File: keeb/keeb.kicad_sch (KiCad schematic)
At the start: 162 parts, among them J101 AVR-ISP-6, J102 USB_C_Receptacle_USB2.0, SW101 SW_Push, SW102 SW_Push, SW103 SW_Push, SW104 SW_Push, SW105 SW_Push, SW106 SW_Push, SW107 SW_Push, SW108 SW_Push, SW109 SW_Push, SW110 SW_Push, SW111 SW_Push, SW112 SW_Push, SW113 SW_Push, SW114 SW_Push, SW115 SW_Push, SW116 SW_Push, SW117 SW_Push, SW118 SW_Push, SW119 SW_Push, SW120 SW_Push, SW121 SW_Push, SW122 SW_Push, SW123 SW_Push, SW124 SW_Push, SW125 SW_Push, SW126 SW_Push, SW127 SW_Push, SW128 SW_Push, SW129 SW_Push, SW130 SW_Push, SW131 SW_Push, SW132 SW_Push, SW133 SW_Push, SW134 SW_Push, SW135 SW_Push, SW136 SW_Push, SW137 SW_Push, SW138 SW_Push, SW139 SW_Push, SW140 SW_Push, SW141 SW_Push, SW142 SW_Push, SW143 SW_Push, SW144 SW_Push, SW145 SW_Push, SW146 SW_Push, SW147 SW_Push, SW148 SW_Push, SW149 SW_Push, SW150 SW_Push, SW151 SW_Push, SW152 SW_Push, SW153 SW_Push, SW154 SW_Push, SW155 SW_Push, SW156 SW_Push, SW157 SW_Push, SW158 SW_Push, SW159 SW_Push, SW160 SW_Push, SW161 SW_Push, SW162 SW_Push, SW163 SW_Push, SW164 SW_Push, SW165 SW_Push, SW166 SW_Push, SW167 SW_Push, U1 TPD2S017, U101 ATmega32U4-AU, Y101 16Mhz

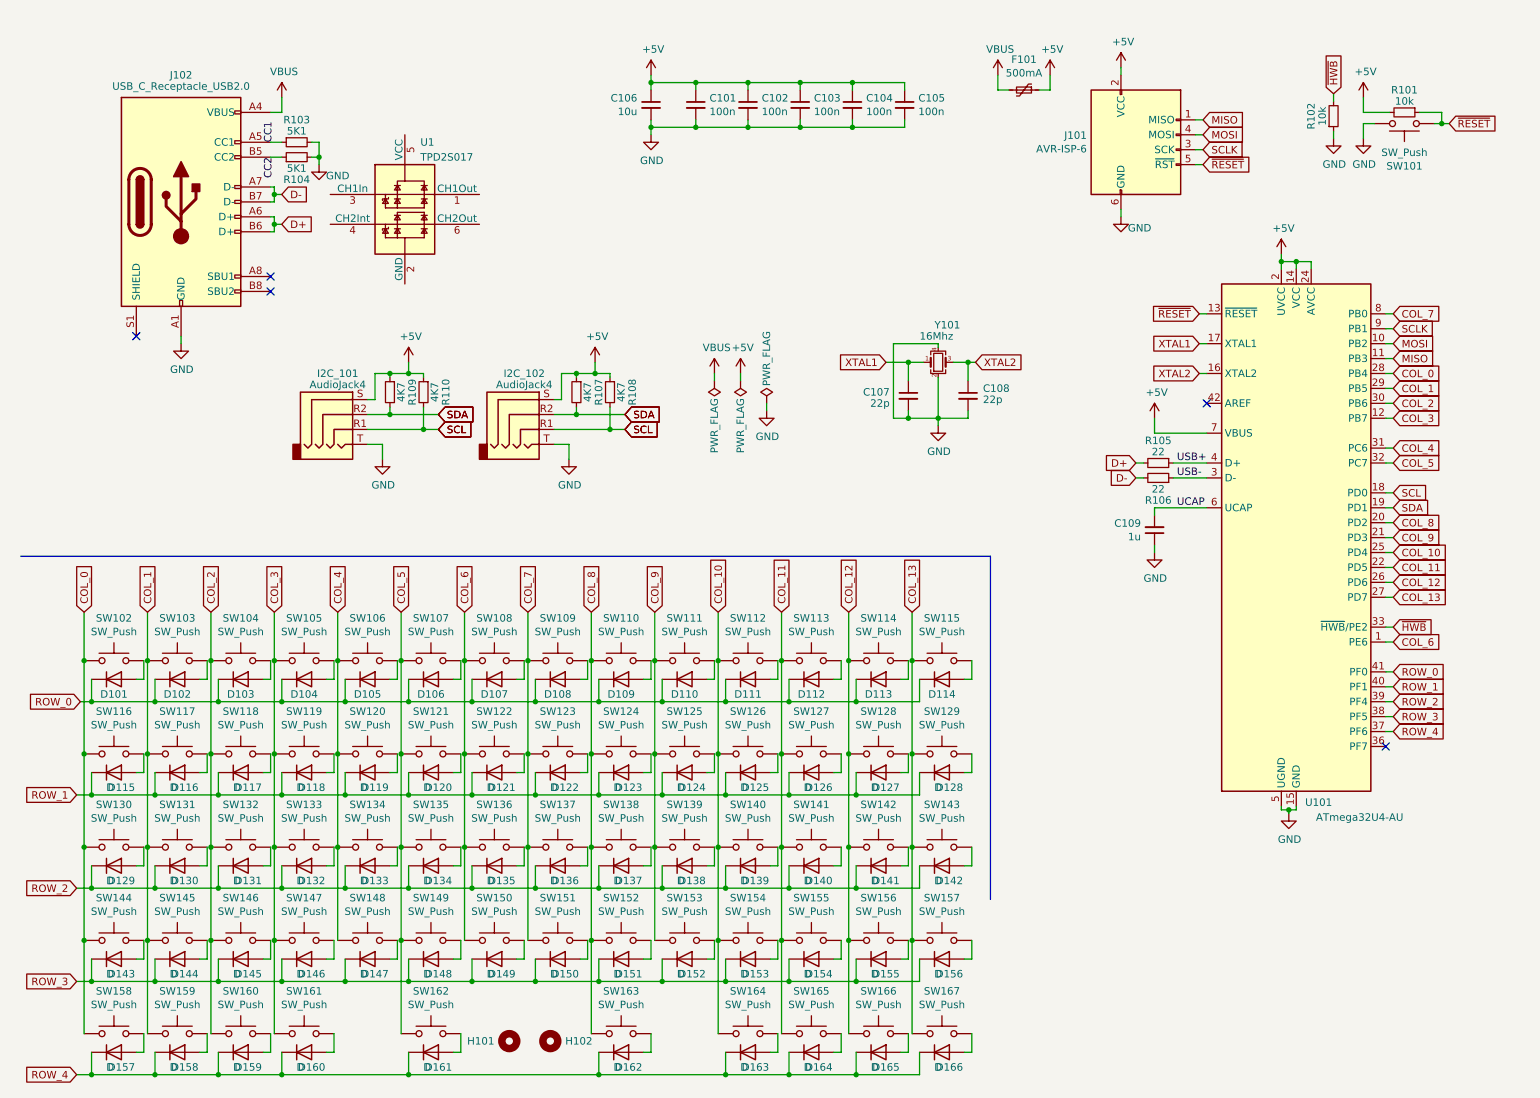
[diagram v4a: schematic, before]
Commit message: footprints/general libs redone
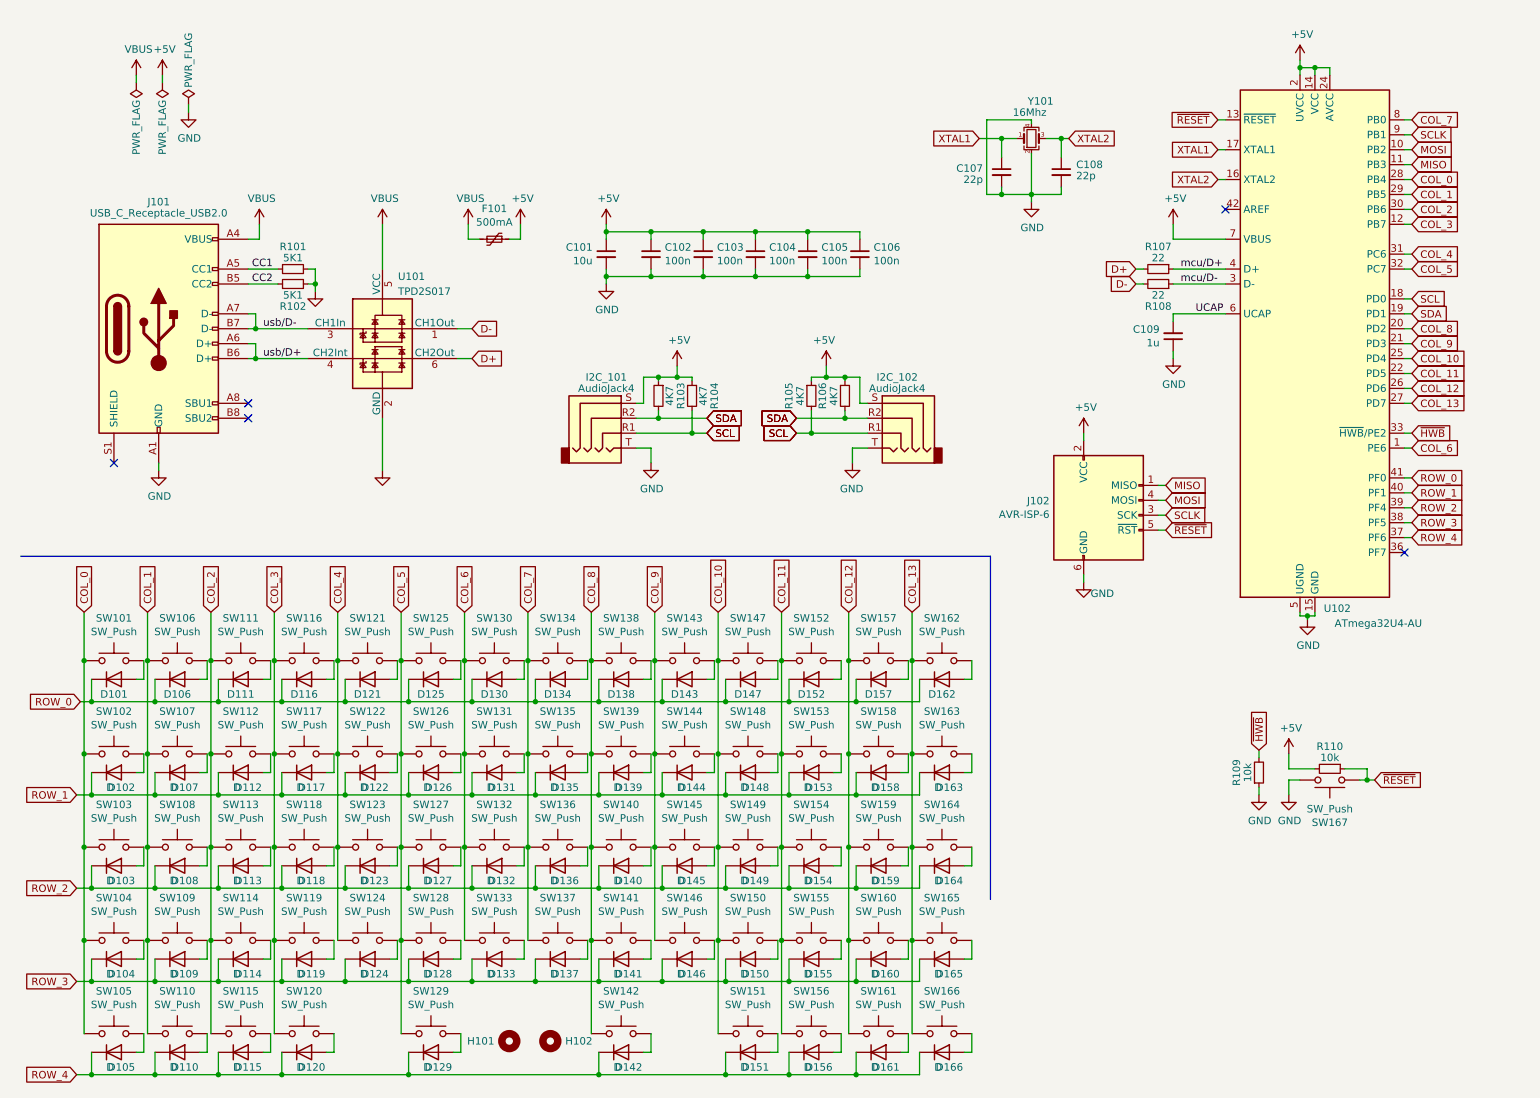
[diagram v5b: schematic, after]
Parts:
- D101, D136, D166: footprint Diode_SMD:D_SOD-123F -> Diode_SMD:D_SOD-323F
- D102: renamed from D115; footprint Diode_SMD:D_SOD-123F -> Diode_SMD:D_SOD-323F
- D103: renamed from D129; footprint Diode_SMD:D_SOD-123F -> Diode_SMD:D_SOD-323F
- D104: renamed from D143; footprint Diode_SMD:D_SOD-123F -> Diode_SMD:D_SOD-323F
- D105: renamed from D157; footprint Diode_SMD:D_SOD-123F -> Diode_SMD:D_SOD-323F
- D106: renamed from D102; footprint Diode_SMD:D_SOD-123F -> Diode_SMD:D_SOD-323F
- D107: renamed from D116; footprint Diode_SMD:D_SOD-123F -> Diode_SMD:D_SOD-323F
- D108: renamed from D130; footprint Diode_SMD:D_SOD-123F -> Diode_SMD:D_SOD-323F
- D109: renamed from D144; footprint Diode_SMD:D_SOD-123F -> Diode_SMD:D_SOD-323F
- D110: renamed from D158; footprint Diode_SMD:D_SOD-123F -> Diode_SMD:D_SOD-323F
- D111: renamed from D103; footprint Diode_SMD:D_SOD-123F -> Diode_SMD:D_SOD-323F
- D112: renamed from D117; footprint Diode_SMD:D_SOD-123F -> Diode_SMD:D_SOD-323F
- D113: renamed from D131; footprint Diode_SMD:D_SOD-123F -> Diode_SMD:D_SOD-323F
- D114: renamed from D145; footprint Diode_SMD:D_SOD-123F -> Diode_SMD:D_SOD-323F
- D115: renamed from D159; footprint Diode_SMD:D_SOD-123F -> Diode_SMD:D_SOD-323F
- D116: renamed from D104; footprint Diode_SMD:D_SOD-123F -> Diode_SMD:D_SOD-323F
- D117: renamed from D118; footprint Diode_SMD:D_SOD-123F -> Diode_SMD:D_SOD-323F
- D118: renamed from D132; footprint Diode_SMD:D_SOD-123F -> Diode_SMD:D_SOD-323F
- D119: renamed from D146; footprint Diode_SMD:D_SOD-123F -> Diode_SMD:D_SOD-323F
- D120: renamed from D160; footprint Diode_SMD:D_SOD-123F -> Diode_SMD:D_SOD-323F
- D121: renamed from D105; footprint Diode_SMD:D_SOD-123F -> Diode_SMD:D_SOD-323F
- D122: renamed from D119; footprint Diode_SMD:D_SOD-123F -> Diode_SMD:D_SOD-323F
- D123: renamed from D133; footprint Diode_SMD:D_SOD-123F -> Diode_SMD:D_SOD-323F
- D124: renamed from D147; footprint Diode_SMD:D_SOD-123F -> Diode_SMD:D_SOD-323F
- D125: renamed from D106; footprint Diode_SMD:D_SOD-123F -> Diode_SMD:D_SOD-323F
- D126: renamed from D120; footprint Diode_SMD:D_SOD-123F -> Diode_SMD:D_SOD-323F
- D127: renamed from D134; footprint Diode_SMD:D_SOD-123F -> Diode_SMD:D_SOD-323F
- D128: renamed from D148; footprint Diode_SMD:D_SOD-123F -> Diode_SMD:D_SOD-323F
- D129: renamed from D161; footprint Diode_SMD:D_SOD-123F -> Diode_SMD:D_SOD-323F
- D130: renamed from D107; footprint Diode_SMD:D_SOD-123F -> Diode_SMD:D_SOD-323F
- D131: renamed from D121; footprint Diode_SMD:D_SOD-123F -> Diode_SMD:D_SOD-323F
- D132: renamed from D135; footprint Diode_SMD:D_SOD-123F -> Diode_SMD:D_SOD-323F
- D133: renamed from D149; footprint Diode_SMD:D_SOD-123F -> Diode_SMD:D_SOD-323F
- D134: renamed from D108; footprint Diode_SMD:D_SOD-123F -> Diode_SMD:D_SOD-323F
- D135: renamed from D122; footprint Diode_SMD:D_SOD-123F -> Diode_SMD:D_SOD-323F
- D137: renamed from D150; footprint Diode_SMD:D_SOD-123F -> Diode_SMD:D_SOD-323F
- D138: renamed from D109; footprint Diode_SMD:D_SOD-123F -> Diode_SMD:D_SOD-323F
- D139: renamed from D123; footprint Diode_SMD:D_SOD-123F -> Diode_SMD:D_SOD-323F
- D140: renamed from D137; footprint Diode_SMD:D_SOD-123F -> Diode_SMD:D_SOD-323F
- D141: renamed from D151; footprint Diode_SMD:D_SOD-123F -> Diode_SMD:D_SOD-323F
- D142: renamed from D162; footprint Diode_SMD:D_SOD-123F -> Diode_SMD:D_SOD-323F
- D143: renamed from D110; footprint Diode_SMD:D_SOD-123F -> Diode_SMD:D_SOD-323F
- D144: renamed from D124; footprint Diode_SMD:D_SOD-123F -> Diode_SMD:D_SOD-323F
- D145: renamed from D138; footprint Diode_SMD:D_SOD-123F -> Diode_SMD:D_SOD-323F
- D146: renamed from D152; footprint Diode_SMD:D_SOD-123F -> Diode_SMD:D_SOD-323F
- D147: renamed from D111; footprint Diode_SMD:D_SOD-123F -> Diode_SMD:D_SOD-323F
- D148: renamed from D125; footprint Diode_SMD:D_SOD-123F -> Diode_SMD:D_SOD-323F
- D149: renamed from D139; footprint Diode_SMD:D_SOD-123F -> Diode_SMD:D_SOD-323F
- D150: renamed from D153; footprint Diode_SMD:D_SOD-123F -> Diode_SMD:D_SOD-323F
- D151: renamed from D163; footprint Diode_SMD:D_SOD-123F -> Diode_SMD:D_SOD-323F
- D152: renamed from D112; footprint Diode_SMD:D_SOD-123F -> Diode_SMD:D_SOD-323F
- D153: renamed from D126; footprint Diode_SMD:D_SOD-123F -> Diode_SMD:D_SOD-323F
- D154: renamed from D140; footprint Diode_SMD:D_SOD-123F -> Diode_SMD:D_SOD-323F
- D155: renamed from D154; footprint Diode_SMD:D_SOD-123F -> Diode_SMD:D_SOD-323F
- D156: renamed from D164; footprint Diode_SMD:D_SOD-123F -> Diode_SMD:D_SOD-323F
- D157: renamed from D113; footprint Diode_SMD:D_SOD-123F -> Diode_SMD:D_SOD-323F
- D158: renamed from D127; footprint Diode_SMD:D_SOD-123F -> Diode_SMD:D_SOD-323F
- D159: renamed from D141; footprint Diode_SMD:D_SOD-123F -> Diode_SMD:D_SOD-323F
- D160: renamed from D155; footprint Diode_SMD:D_SOD-123F -> Diode_SMD:D_SOD-323F
- D161: renamed from D165; footprint Diode_SMD:D_SOD-123F -> Diode_SMD:D_SOD-323F
- D162: renamed from D114; footprint Diode_SMD:D_SOD-123F -> Diode_SMD:D_SOD-323F
- D163: renamed from D128; footprint Diode_SMD:D_SOD-123F -> Diode_SMD:D_SOD-323F
- D164: renamed from D142; footprint Diode_SMD:D_SOD-123F -> Diode_SMD:D_SOD-323F
- D165: renamed from D156; footprint Diode_SMD:D_SOD-123F -> Diode_SMD:D_SOD-323F
- H101, H102: footprint Mounting_Keyboard_Stabilizer:Stabilizer_Cherry_MX_3u -> PCM_Mounting_Keyboard_Stabilizer:Stabilizer_Cherry_MX_3.00u
- SW102: renamed from SW116; footprint Switch_Keyboard_Cherry_MX:SW_Cherry_MX_PCB_1.00u -> PCM_Switch_Keyboard_Cherry_MX:SW_Cherry_MX_PCB_1.00u
- SW103: renamed from SW130; footprint Switch_Keyboard_Cherry_MX:SW_Cherry_MX_PCB_1.00u -> PCM_Switch_Keyboard_Cherry_MX:SW_Cherry_MX_PCB_1.00u
- SW104: renamed from SW144; footprint Switch_Keyboard_Cherry_MX:SW_Cherry_MX_PCB_1.00u -> PCM_Switch_Keyboard_Cherry_MX:SW_Cherry_MX_PCB_1.00u
- SW105: renamed from SW158; footprint Switch_Keyboard_Cherry_MX:SW_Cherry_MX_PCB_1.00u -> PCM_Switch_Keyboard_Cherry_MX:SW_Cherry_MX_PCB_1.00u
- SW106: renamed from SW103; footprint Switch_Keyboard_Cherry_MX:SW_Cherry_MX_PCB_1.00u -> PCM_Switch_Keyboard_Cherry_MX:SW_Cherry_MX_PCB_1.00u
- SW107: renamed from SW117; footprint Switch_Keyboard_Cherry_MX:SW_Cherry_MX_PCB_1.00u -> PCM_Switch_Keyboard_Cherry_MX:SW_Cherry_MX_PCB_1.00u
- SW108: renamed from SW131; footprint Switch_Keyboard_Cherry_MX:SW_Cherry_MX_PCB_1.00u -> PCM_Switch_Keyboard_Cherry_MX:SW_Cherry_MX_PCB_1.00u
- SW109: renamed from SW145; footprint Switch_Keyboard_Cherry_MX:SW_Cherry_MX_PCB_1.00u -> PCM_Switch_Keyboard_Cherry_MX:SW_Cherry_MX_PCB_1.00u
- SW110: renamed from SW159; footprint Switch_Keyboard_Cherry_MX:SW_Cherry_MX_PCB_1.00u -> PCM_Switch_Keyboard_Cherry_MX:SW_Cherry_MX_PCB_1.00u
- SW111: renamed from SW104; footprint Switch_Keyboard_Cherry_MX:SW_Cherry_MX_PCB_1.00u -> PCM_Switch_Keyboard_Cherry_MX:SW_Cherry_MX_PCB_1.00u
- SW112: renamed from SW118; footprint Switch_Keyboard_Cherry_MX:SW_Cherry_MX_PCB_1.00u -> PCM_Switch_Keyboard_Cherry_MX:SW_Cherry_MX_PCB_1.00u
- SW113: renamed from SW132; footprint Switch_Keyboard_Cherry_MX:SW_Cherry_MX_PCB_1.00u -> PCM_Switch_Keyboard_Cherry_MX:SW_Cherry_MX_PCB_1.00u
- SW114: renamed from SW146; footprint Switch_Keyboard_Cherry_MX:SW_Cherry_MX_PCB_1.00u -> PCM_Switch_Keyboard_Cherry_MX:SW_Cherry_MX_PCB_1.00u
- SW115: renamed from SW160; footprint Switch_Keyboard_Cherry_MX:SW_Cherry_MX_PCB_1.00u -> PCM_Switch_Keyboard_Cherry_MX:SW_Cherry_MX_PCB_1.00u
- SW116: renamed from SW105; footprint Switch_Keyboard_Cherry_MX:SW_Cherry_MX_PCB_1.00u -> PCM_Switch_Keyboard_Cherry_MX:SW_Cherry_MX_PCB_1.00u
- SW117: renamed from SW119; footprint Switch_Keyboard_Cherry_MX:SW_Cherry_MX_PCB_1.00u -> PCM_Switch_Keyboard_Cherry_MX:SW_Cherry_MX_PCB_1.00u
- SW118: renamed from SW133; footprint Switch_Keyboard_Cherry_MX:SW_Cherry_MX_PCB_1.00u -> PCM_Switch_Keyboard_Cherry_MX:SW_Cherry_MX_PCB_1.00u
- SW119: renamed from SW147; footprint Switch_Keyboard_Cherry_MX:SW_Cherry_MX_PCB_1.00u -> PCM_Switch_Keyboard_Cherry_MX:SW_Cherry_MX_PCB_1.00u
- SW120: renamed from SW161; footprint Switch_Keyboard_Cherry_MX:SW_Cherry_MX_PCB_1.00u -> PCM_Switch_Keyboard_Cherry_MX:SW_Cherry_MX_PCB_1.00u
- SW121: renamed from SW106; footprint Switch_Keyboard_Cherry_MX:SW_Cherry_MX_PCB_1.00u -> PCM_Switch_Keyboard_Cherry_MX:SW_Cherry_MX_PCB_1.00u
- SW122: renamed from SW120; footprint Switch_Keyboard_Cherry_MX:SW_Cherry_MX_PCB_1.00u -> PCM_Switch_Keyboard_Cherry_MX:SW_Cherry_MX_PCB_1.00u
- SW123: renamed from SW134; footprint Switch_Keyboard_Cherry_MX:SW_Cherry_MX_PCB_1.00u -> PCM_Switch_Keyboard_Cherry_MX:SW_Cherry_MX_PCB_1.00u
- SW124: renamed from SW148; footprint Switch_Keyboard_Cherry_MX:SW_Cherry_MX_PCB_1.00u -> PCM_Switch_Keyboard_Cherry_MX:SW_Cherry_MX_PCB_1.00u
- SW125: renamed from SW107; footprint Switch_Keyboard_Cherry_MX:SW_Cherry_MX_PCB_1.00u -> PCM_Switch_Keyboard_Cherry_MX:SW_Cherry_MX_PCB_1.00u
- SW126: renamed from SW121; footprint Switch_Keyboard_Cherry_MX:SW_Cherry_MX_PCB_1.00u -> PCM_Switch_Keyboard_Cherry_MX:SW_Cherry_MX_PCB_1.00u
- SW127: renamed from SW135; footprint Switch_Keyboard_Cherry_MX:SW_Cherry_MX_PCB_1.00u -> PCM_Switch_Keyboard_Cherry_MX:SW_Cherry_MX_PCB_1.00u
- SW128: renamed from SW149; footprint Switch_Keyboard_Cherry_MX:SW_Cherry_MX_PCB_1.00u -> PCM_Switch_Keyboard_Cherry_MX:SW_Cherry_MX_PCB_1.00u
- SW129: renamed from SW162; footprint Switch_Keyboard_Cherry_MX:SW_Cherry_MX_PCB_3.00u -> PCM_Switch_Keyboard_Cherry_MX:SW_Cherry_MX_PCB_3.00u
- SW130: renamed from SW108; footprint Switch_Keyboard_Cherry_MX:SW_Cherry_MX_PCB_1.00u -> PCM_Switch_Keyboard_Cherry_MX:SW_Cherry_MX_PCB_1.00u
- SW131: renamed from SW122; footprint Switch_Keyboard_Cherry_MX:SW_Cherry_MX_PCB_1.00u -> PCM_Switch_Keyboard_Cherry_MX:SW_Cherry_MX_PCB_1.00u
- SW132: renamed from SW136; footprint Switch_Keyboard_Cherry_MX:SW_Cherry_MX_PCB_1.00u -> PCM_Switch_Keyboard_Cherry_MX:SW_Cherry_MX_PCB_1.00u
- SW133: renamed from SW150; footprint Switch_Keyboard_Cherry_MX:SW_Cherry_MX_PCB_1.00u -> PCM_Switch_Keyboard_Cherry_MX:SW_Cherry_MX_PCB_1.00u
- SW134: renamed from SW109; footprint Switch_Keyboard_Cherry_MX:SW_Cherry_MX_PCB_1.00u -> PCM_Switch_Keyboard_Cherry_MX:SW_Cherry_MX_PCB_1.00u
- SW135: renamed from SW123; footprint Switch_Keyboard_Cherry_MX:SW_Cherry_MX_PCB_1.00u -> PCM_Switch_Keyboard_Cherry_MX:SW_Cherry_MX_PCB_1.00u
- SW136: renamed from SW137; footprint Switch_Keyboard_Cherry_MX:SW_Cherry_MX_PCB_1.00u -> PCM_Switch_Keyboard_Cherry_MX:SW_Cherry_MX_PCB_1.00u
- SW137: renamed from SW151; footprint Switch_Keyboard_Cherry_MX:SW_Cherry_MX_PCB_1.00u -> PCM_Switch_Keyboard_Cherry_MX:SW_Cherry_MX_PCB_1.00u
- SW138: renamed from SW110; footprint Switch_Keyboard_Cherry_MX:SW_Cherry_MX_PCB_1.00u -> PCM_Switch_Keyboard_Cherry_MX:SW_Cherry_MX_PCB_1.00u
- SW139: renamed from SW124; footprint Switch_Keyboard_Cherry_MX:SW_Cherry_MX_PCB_1.00u -> PCM_Switch_Keyboard_Cherry_MX:SW_Cherry_MX_PCB_1.00u
- SW140: renamed from SW138; footprint Switch_Keyboard_Cherry_MX:SW_Cherry_MX_PCB_1.00u -> PCM_Switch_Keyboard_Cherry_MX:SW_Cherry_MX_PCB_1.00u
- SW141: renamed from SW152; footprint Switch_Keyboard_Cherry_MX:SW_Cherry_MX_PCB_1.00u -> PCM_Switch_Keyboard_Cherry_MX:SW_Cherry_MX_PCB_1.00u
- SW142: renamed from SW163; footprint Switch_Keyboard_Cherry_MX:SW_Cherry_MX_PCB_3.00u -> PCM_Switch_Keyboard_Cherry_MX:SW_Cherry_MX_PCB_3.00u
- SW143: renamed from SW111; footprint Switch_Keyboard_Cherry_MX:SW_Cherry_MX_PCB_1.00u -> PCM_Switch_Keyboard_Cherry_MX:SW_Cherry_MX_PCB_1.00u
- SW144: renamed from SW125; footprint Switch_Keyboard_Cherry_MX:SW_Cherry_MX_PCB_1.00u -> PCM_Switch_Keyboard_Cherry_MX:SW_Cherry_MX_PCB_1.00u
- SW145: renamed from SW139; footprint Switch_Keyboard_Cherry_MX:SW_Cherry_MX_PCB_1.00u -> PCM_Switch_Keyboard_Cherry_MX:SW_Cherry_MX_PCB_1.00u
- SW146: renamed from SW153; footprint Switch_Keyboard_Cherry_MX:SW_Cherry_MX_PCB_1.00u -> PCM_Switch_Keyboard_Cherry_MX:SW_Cherry_MX_PCB_1.00u
- SW147: renamed from SW112; footprint Switch_Keyboard_Cherry_MX:SW_Cherry_MX_PCB_1.00u -> PCM_Switch_Keyboard_Cherry_MX:SW_Cherry_MX_PCB_1.00u
- SW148: renamed from SW126; footprint Switch_Keyboard_Cherry_MX:SW_Cherry_MX_PCB_1.00u -> PCM_Switch_Keyboard_Cherry_MX:SW_Cherry_MX_PCB_1.00u
- SW149: renamed from SW140; footprint Switch_Keyboard_Cherry_MX:SW_Cherry_MX_PCB_1.00u -> PCM_Switch_Keyboard_Cherry_MX:SW_Cherry_MX_PCB_1.00u
- SW150: renamed from SW154; footprint Switch_Keyboard_Cherry_MX:SW_Cherry_MX_PCB_1.00u -> PCM_Switch_Keyboard_Cherry_MX:SW_Cherry_MX_PCB_1.00u
- SW151: renamed from SW164; footprint Switch_Keyboard_Cherry_MX:SW_Cherry_MX_PCB_1.00u -> PCM_Switch_Keyboard_Cherry_MX:SW_Cherry_MX_PCB_1.00u
- SW152: renamed from SW113; footprint Switch_Keyboard_Cherry_MX:SW_Cherry_MX_PCB_1.00u -> PCM_Switch_Keyboard_Cherry_MX:SW_Cherry_MX_PCB_1.00u
- SW153: renamed from SW127; footprint Switch_Keyboard_Cherry_MX:SW_Cherry_MX_PCB_1.00u -> PCM_Switch_Keyboard_Cherry_MX:SW_Cherry_MX_PCB_1.00u
- SW154: renamed from SW141; footprint Switch_Keyboard_Cherry_MX:SW_Cherry_MX_PCB_1.00u -> PCM_Switch_Keyboard_Cherry_MX:SW_Cherry_MX_PCB_1.00u
- SW155: footprint Switch_Keyboard_Cherry_MX:SW_Cherry_MX_PCB_1.00u -> PCM_Switch_Keyboard_Cherry_MX:SW_Cherry_MX_PCB_1.00u
- SW156: renamed from SW165; footprint Switch_Keyboard_Cherry_MX:SW_Cherry_MX_PCB_1.00u -> PCM_Switch_Keyboard_Cherry_MX:SW_Cherry_MX_PCB_1.00u
- SW157: renamed from SW114; footprint Switch_Keyboard_Cherry_MX:SW_Cherry_MX_PCB_1.00u -> PCM_Switch_Keyboard_Cherry_MX:SW_Cherry_MX_PCB_1.00u
- SW158: renamed from SW128; footprint Switch_Keyboard_Cherry_MX:SW_Cherry_MX_PCB_1.00u -> PCM_Switch_Keyboard_Cherry_MX:SW_Cherry_MX_PCB_1.00u
- SW159: renamed from SW142; footprint Switch_Keyboard_Cherry_MX:SW_Cherry_MX_PCB_1.00u -> PCM_Switch_Keyboard_Cherry_MX:SW_Cherry_MX_PCB_1.00u
- SW160: renamed from SW156; footprint Switch_Keyboard_Cherry_MX:SW_Cherry_MX_PCB_1.00u -> PCM_Switch_Keyboard_Cherry_MX:SW_Cherry_MX_PCB_1.00u
- SW161: renamed from SW166; footprint Switch_Keyboard_Cherry_MX:SW_Cherry_MX_PCB_1.00u -> PCM_Switch_Keyboard_Cherry_MX:SW_Cherry_MX_PCB_1.00u
- SW162: renamed from SW115; footprint Switch_Keyboard_Cherry_MX:SW_Cherry_MX_PCB_1.00u -> PCM_Switch_Keyboard_Cherry_MX:SW_Cherry_MX_PCB_1.00u
- SW163: renamed from SW129; footprint Switch_Keyboard_Cherry_MX:SW_Cherry_MX_PCB_1.00u -> PCM_Switch_Keyboard_Cherry_MX:SW_Cherry_MX_PCB_1.00u
- SW164: renamed from SW143; footprint Switch_Keyboard_Cherry_MX:SW_Cherry_MX_PCB_1.00u -> PCM_Switch_Keyboard_Cherry_MX:SW_Cherry_MX_PCB_1.00u
- SW165: renamed from SW157; footprint Switch_Keyboard_Cherry_MX:SW_Cherry_MX_PCB_1.00u -> PCM_Switch_Keyboard_Cherry_MX:SW_Cherry_MX_PCB_1.00u
- SW166: renamed from SW167; footprint Switch_Keyboard_Cherry_MX:SW_Cherry_MX_PCB_1.00u -> PCM_Switch_Keyboard_Cherry_MX:SW_Cherry_MX_PCB_1.00u
- renumbered C106 to C101, C101 to C102, C102 to C103, C103 to C104, C104 to C105, C105 to C106, I2C_102 to I2C_101, I2C_101 to I2C_102, J102 to J101, J101 to J102, R103 to R101, R104 to R102, R107 to R103, R108 to R104, R110 to R105, R109 to R106, R105 to R107, R106 to R108, R102 to R109, R101 to R110, SW102 to SW101, SW101 to SW167, U1 to U101, U101 to U102
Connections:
- net D+: now also U101.6 (CH2Out); no longer J101.A6 (D+), J101.B6 (D+)
- net D-: now also U101.1 (CH1Out); no longer J101.A7 (D-), J101.B7 (D-)
- net GND: now also U101.2 (GND)
- net VBUS: now also U101.5 (VCC)
- net usb/D-: now reaches U101.3 (CH1In)
- net usb/D-: now also J101.A7 (D-), J101.B7 (D-)
- net usb/D+: now reaches U101.4 (CH2Int)
- net usb/D+: now also J101.A6 (D+), J101.B6 (D+)
- net USB+ renamed mcu/D+
- net USB- renamed mcu/D-
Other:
- moved on the sheet: C101, C102, C103, C104, C105, C106, C107, C108, C109, F101, I2C_101, I2C_102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

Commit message: matrix and row/colrouting
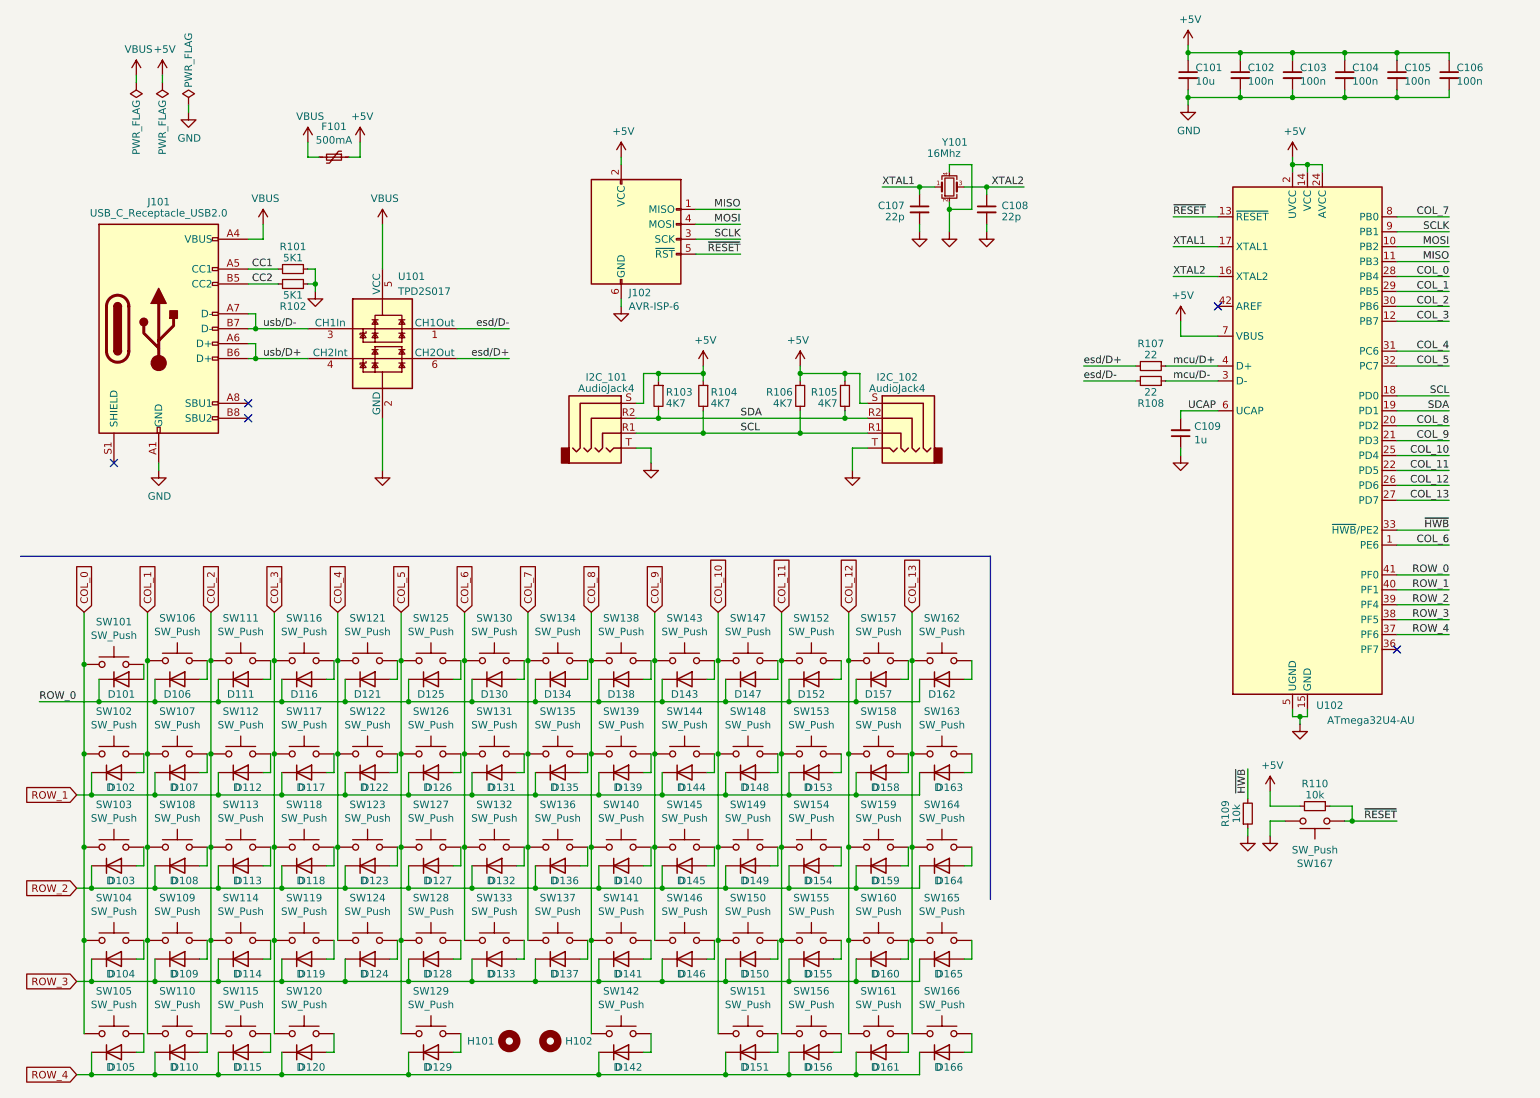
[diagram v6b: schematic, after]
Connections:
- net SCL: now also R106.2; no longer R105.2
- net SDA: now also R105.2; no longer R106.2
- net D+ renamed esd/D+
- net D- renamed esd/D-
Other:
- moved on the sheet: C101, C102, C103, C104, C105, C106, C107, C108, C109, D101, F101, J102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

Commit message: USB
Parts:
- C102, C103, C104, C105, C106, C107, C108, C109: footprint Capacitor_SMD:C_0603_1608Metric_Pad1.08x0.95mm_HandSolder -> Capacitor_SMD:C_0402_1005Metric
- R101, R102, R103, R104, R105, R106, R107, R108, R109, R110: footprint Resistor_SMD:R_0603_1608Metric_Pad0.98x0.95mm_HandSolder -> Resistor_SMD:R_0402_1005Metric
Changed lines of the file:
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@@
       (effects (font (size 1.27 1.27)))
     )
-    (property "Footprint" "Resistor_SMD:R_0603_1608Metric_Pad0.98x0.95mm_HandSolder" (at 204.47 74.93 0)
+    (property "Footprint" "Resistor_SMD:R_0402_1005Metric" (at 204.47 74.93 0)
       (effects (font (size 1.27 1.27)) hide)
     )
@@
       (effects (font (size 1.27 1.27)))
     )
-    (property "Footprint" "Resistor_SMD:R_0603_1608Metric_Pad0.98x0.95mm_HandSolder" (at 204.47 77.47 0)
+    (property "Footprint" "Resistor_SMD:R_0402_1005Metric" (at 204.47 77.47 0)
       (effects (font (size 1.27 1.27)) hide)
     )
@@
       (effects (font (size 1.27 1.27)) (justify right))
     )
-    (property "Footprint" "Resistor_SMD:R_0603_1608Metric_Pad0.98x0.95mm_HandSolder" (at 120.65 80.01 0)
+    (property "Footprint" "Resistor_SMD:R_0402_1005Metric" (at 120.65 80.01 0)
       (effects (font (size 1.27 1.27)) hide)
     )
@@
       (effects (font (size 1.27 1.27)))
     )
-    (property "Footprint" "Resistor_SMD:R_0603_1608Metric_Pad0.98x0.95mm_HandSolder" (at 58.42 60.96 0)
+    (property "Footprint" "Resistor_SMD:R_0402_1005Metric" (at 58.42 60.96 0)
       (effects (font (size 1.27 1.27)) hide)
     )
@@
       (effects (font (size 1.27 1.27)))
     )
-    (property "Footprint" "Resistor_SMD:R_0603_1608Metric_Pad0.98x0.95mm_HandSolder" (at 58.42 58.42 0)
+    (property "Footprint" "Resistor_SMD:R_0402_1005Metric" (at 58.42 58.42 0)
       (effects (font (size 1.27 1.27)) hide)
     )
@@
       (effects (font (size 1.27 1.27)) (justify right))
     )
-    (property "Footprint" "Capacitor_SMD:C_0603_1608Metric_Pad1.08x0.95mm_HandSolder" (at 209.55 86.36 0)
+    (property "Footprint" "Capacitor_SMD:C_0402_1005Metric" (at 209.55 86.36 0)
       (effects (font (size 1.27 1.27)) hide)
     )
@@
       (effects (font (size 1.27 1.27)) (justify left))
     )
-    (property "Footprint" "Capacitor_SMD:C_0603_1608Metric_Pad1.08x0.95mm_HandSolder" (at 219.71 25.4 0)
+    (property "Footprint" "Capacitor_SMD:C_0402_1005Metric" (at 219.71 25.4 0)
       (effects (font (size 1.27 1.27)) hide)
     )
@@
       (effects (font (size 1.27 1.27)) (justify left))
     )
-    (property "Footprint" "Capacitor_SMD:C_0603_1608Metric_Pad1.08x0.95mm_HandSolder" (at 228.6 25.4 0)
+    (property "Footprint" "Capacitor_SMD:C_0402_1005Metric" (at 228.6 25.4 0)
       (effects (font (size 1.27 1.27)) hide)
     )
@@
       (effects (font (size 1.27 1.27)) (justify left))
     )
-    (property "Footprint" "Capacitor_SMD:C_0603_1608Metric_Pad1.08x0.95mm_HandSolder" (at 237.49 25.4 0)
+    (property "Footprint" "Capacitor_SMD:C_0402_1005Metric" (at 237.49 25.4 0)
       (effects (font (size 1.27 1.27)) hide)
     )
@@
       (effects (font (size 1.27 1.27)) (justify left))
     )
-    (property "Footprint" "Capacitor_SMD:C_0603_1608Metric_Pad1.08x0.95mm_HandSolder" (at 246.38 25.4 0)
+    (property "Footprint" "Capacitor_SMD:C_0402_1005Metric" (at 246.38 25.4 0)
       (effects (font (size 1.27 1.27)) hide)
     )
@@
       (effects (font (size 1.27 1.27)) (justify left))
     )
-    (property "Footprint" "Capacitor_SMD:C_0603_1608Metric_Pad1.08x0.95mm_HandSolder" (at 255.27 25.4 0)
+    (property "Footprint" "Capacitor_SMD:C_0402_1005Metric" (at 255.27 25.4 0)
       (effects (font (size 1.27 1.27)) hide)
     )
@@
       (effects (font (size 1.27 1.27)) (justify right))
     )
-    (property "Footprint" "Capacitor_SMD:C_0603_1608Metric_Pad1.08x0.95mm_HandSolder" (at 165.1 48.26 0)
+    (property "Footprint" "Capacitor_SMD:C_0402_1005Metric" (at 165.1 48.26 0)
       (effects (font (size 1.27 1.27)) hide)
     )
@@
       (effects (font (size 1.27 1.27)) (justify right))
     )
-    (property "Footprint" "Capacitor_SMD:C_0603_1608Metric_Pad1.08x0.95mm_HandSolder" (at 176.53 48.26 0)
+    (property "Footprint" "Capacitor_SMD:C_0402_1005Metric" (at 176.53 48.26 0)
       (effects (font (size 1.27 1.27)) hide)
     )
@@
       (effects (font (size 1.27 1.27)))
     )
-    (property "Footprint" "Resistor_SMD:R_0603_1608Metric_Pad0.98x0.95mm_HandSolder" (at 232.41 149.86 0)
+    (property "Footprint" "Resistor_SMD:R_0402_1005Metric" (at 232.41 149.86 0)
       (effects (font (size 1.27 1.27)) hide)
     )
@@
       (effects (font (size 1.27 1.27)))
     )
-    (property "Footprint" "Resistor_SMD:R_0603_1608Metric_Pad0.98x0.95mm_HandSolder" (at 220.98 151.13 0)
+    (property "Footprint" "Resistor_SMD:R_0402_1005Metric" (at 220.98 151.13 0)
       (effects (font (size 1.27 1.27)) hide)
     )
@@
       (effects (font (size 1.27 1.27)) (justify right))
     )
-    (property "Footprint" "Resistor_SMD:R_0603_1608Metric_Pad0.98x0.95mm_HandSolder" (at 152.4 80.01 0)
+    (property "Footprint" "Resistor_SMD:R_0402_1005Metric" (at 152.4 80.01 0)
       (effects (font (size 1.27 1.27)) hide)
     )
@@
       (effects (font (size 1.27 1.27)) (justify right))
     )
-    (property "Footprint" "Resistor_SMD:R_0603_1608Metric_Pad0.98x0.95mm_HandSolder" (at 128.27 80.01 0)
+    (property "Footprint" "Resistor_SMD:R_0402_1005Metric" (at 128.27 80.01 0)
       (effects (font (size 1.27 1.27)) hide)
     )
@@
       (effects (font (size 1.27 1.27)) (justify right))
     )
-    (property "Footprint" "Resistor_SMD:R_0603_1608Metric_Pad0.98x0.95mm_HandSolder" (at 144.78 80.01 0)
-      (effects (font (size 1.27 1.27)) hide)
-    )
+    (property "Footprint" "Resistor_SMD:R_0402_1005Metric" (at 144.78 80.01 0)
+      (effects (font (size 1.27 1.27)) hide)
+    )
